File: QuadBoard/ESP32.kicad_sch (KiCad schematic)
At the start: 2 parts, among them J1 Conn_01x06_Pin, U1 ESP32-S3-DevKitC

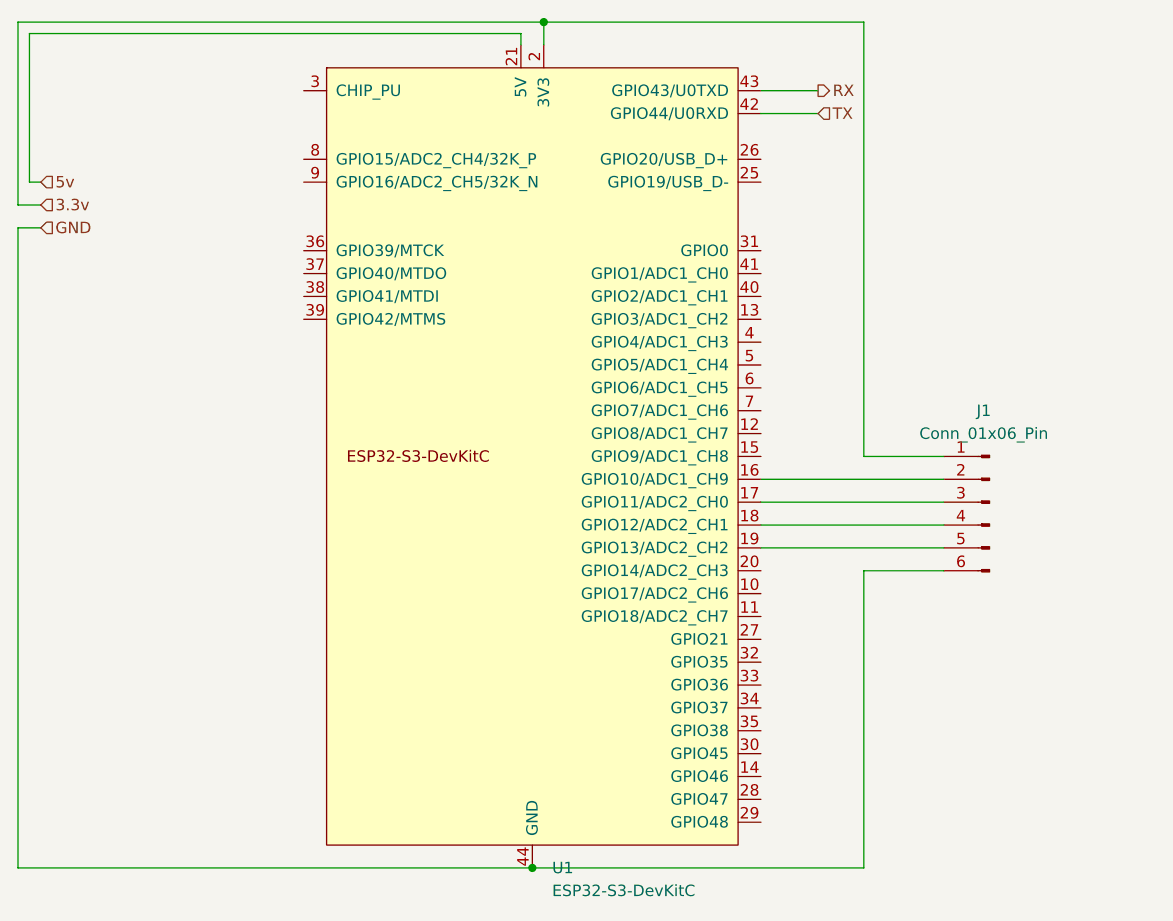
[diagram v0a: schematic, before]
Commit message: Update SD footprint
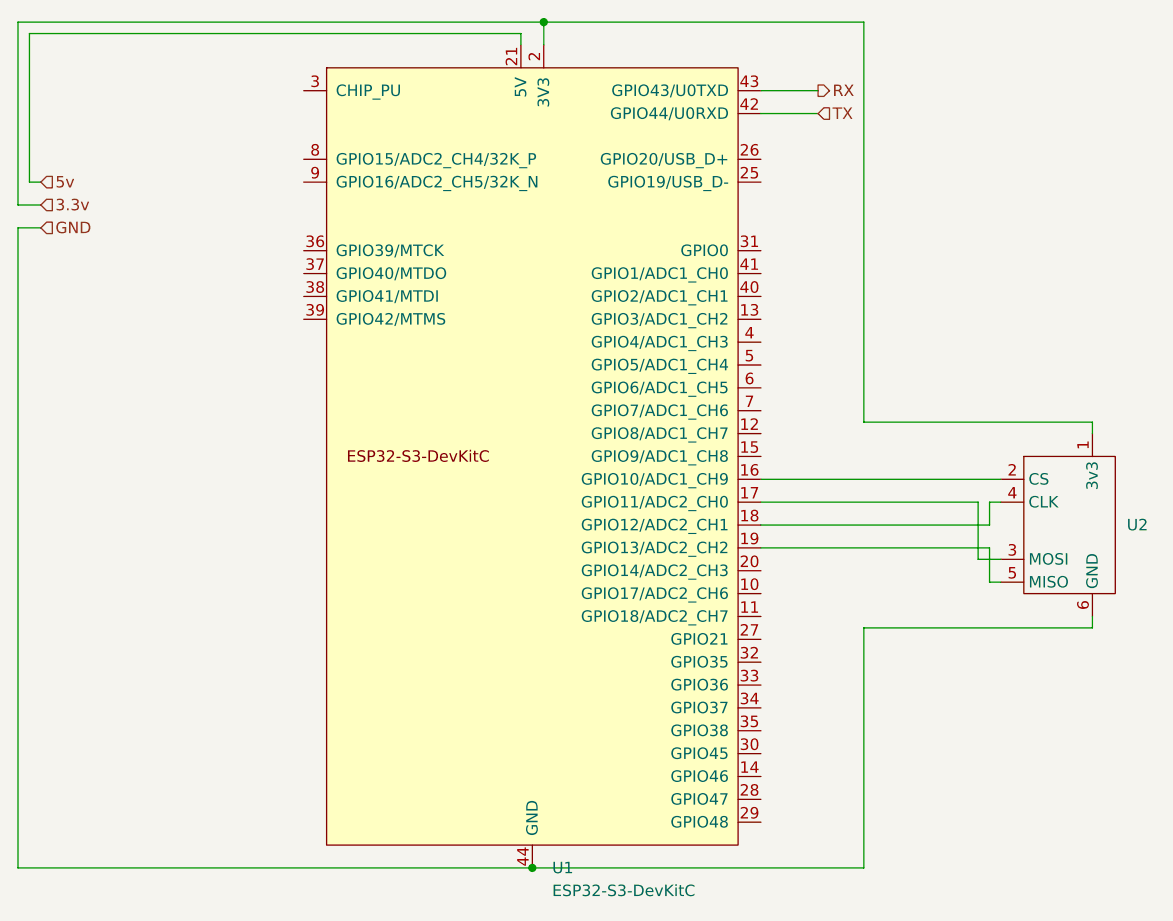
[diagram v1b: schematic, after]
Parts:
- removed J1: Conn_01x06_Pin, Connector_PinHeader_2.54mm:PinHeader_1x06_P2.54mm_Vertical, symbol Connector:Conn_01x06_Pin
- added U2: ~, FlipperLibrary:SD, symbol FlipperLibrary:SD
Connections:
- net 3.3v: now also U2.1 (3v3)
- net GND: now also U2.6 (GND)
- net at U1.16 (GPIO10/ADC1_CH9): now also U2.2 (CS)
- net at U1.17 (GPIO11/ADC2_CH0): now also U2.3 (MOSI)
- net at U1.18 (GPIO12/ADC2_CH1): now also U2.4 (CLK)
- net at U1.19 (GPIO13/ADC2_CH2): now also U2.5 (MISO)
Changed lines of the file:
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@@
   (junction (at 189.23 45.72) (diameter 0) (color 0 0 0 0)
   )
+  (wire (pts (xy 224.79 90.17) (xy 250.19 90.17))
+    (stroke (width 0) (type default))
+  )
   (wire (pts (xy 130.81 45.72) (xy 189.23 45.72))
     (stroke (width 0) (type default))
   )
-  (wire (pts (xy 224.79 93.98) (xy 224.79 45.72))
-    (stroke (width 0) (type default))
-  )
-  (wire (pts (xy 233.68 93.98) (xy 224.79 93.98))
+  (wire (pts (xy 224.79 90.17) (xy 224.79 45.72))
     (stroke (width 0) (type default))
   )
@@
     (stroke (width 0) (type default))
   )
-  (wire (pts (xy 213.36 104.14) (xy 233.68 104.14))
+  (wire (pts (xy 213.36 104.14) (xy 238.76 104.14))
     (stroke (width 0) (type default))
   )
@@
     (stroke (width 0) (type default))
   )
-  (wire (pts (xy 224.79 106.68) (xy 224.79 139.7))
+  (wire (pts (xy 224.79 113.03) (xy 224.79 139.7))
     (stroke (width 0) (type default))
   )
@@
     (stroke (width 0) (type default))
   )
-  (wire (pts (xy 213.36 101.6) (xy 233.68 101.6))
+  (wire (pts (xy 213.36 101.6) (xy 238.76 101.6))
+    (stroke (width 0) (type default))
+  )
+  (wire (pts (xy 238.76 99.06) (xy 240.03 99.06))
     (stroke (width 0) (type default))
   )
@@
     (stroke (width 0) (type default))
   )
-  (wire (pts (xy 233.68 106.68) (xy 224.79 106.68))
-    (stroke (width 0) (type default))
-  )
-  (wire (pts (xy 213.36 99.06) (xy 233.68 99.06))
-    (stroke (width 0) (type default))
-  )
-  (wire (pts (xy 213.36 96.52) (xy 233.68 96.52))
+  (wire (pts (xy 224.79 113.03) (xy 250.19 113.03))
+    (stroke (width 0) (type default))
+  )
+  (wire (pts (xy 238.76 104.14) (xy 238.76 107.95))
+    (stroke (width 0) (type default))
+  )
+  (wire (pts (xy 237.49 105.41) (xy 240.03 105.41))
+    (stroke (width 0) (type default))
+  )
+  (wire (pts (xy 213.36 99.06) (xy 237.49 99.06))
+    (stroke (width 0) (type default))
+  )
+  (wire (pts (xy 250.19 113.03) (xy 250.19 111.76))
+    (stroke (width 0) (type default))
+  )
+  (wire (pts (xy 213.36 96.52) (xy 240.03 96.52))
     (stroke (width 0) (type default))
   )
@@
     (stroke (width 0) (type default))
   )
+  (wire (pts (xy 250.19 90.17) (xy 250.19 91.44))
+    (stroke (width 0) (type default))
+  )
   (wire (pts (xy 130.81 66.04) (xy 130.81 45.72))
     (stroke (width 0) (type default))
   )
+  (wire (pts (xy 237.49 99.06) (xy 237.49 105.41))
+    (stroke (width 0) (type default))
+  )
   (wire (pts (xy 224.79 139.7) (xy 187.96 139.7))
     (stroke (width 0) (type default))
@@
     (stroke (width 0) (type default))
   )
+  (wire (pts (xy 238.76 101.6) (xy 238.76 99.06))
+    (stroke (width 0) (type default))
+  )
+  (wire (pts (xy 238.76 107.95) (xy 240.03 107.95))
+    (stroke (width 0) (type default))
+  )
   (wire (pts (xy 132.08 63.5) (xy 132.08 46.99))
     (stroke (width 0) (type default))
@@
   (hierarchical_label "5v" (shape input) (at 133.35 63.5 0) (fields_autoplaced)
     (effects (font (size 1.27 1.27)) (justify left))
+  )
+  (symbol (lib_id "FlipperLibrary:SD") (at 226.06 93.98 0) (unit 1)
+    (in_bom yes) (on_board yes) (dnp no) (fields_autoplaced)
+    (property "Reference" "U2" (at 254 101.6 0)
+      (effects (font (size 1.27 1.27)) (justify left))
+    )
+    (property "Value" "~" (at 226.06 93.98 0)
+      (effects (font (size 1.27 1.27)))
+    )
+    (property "Footprint" "FlipperLibrary:SD" (at 226.06 93.98 0)
+      (effects (font (size 1.27 1.27)) hide)
+    )
+    (property "Datasheet" "" (at 226.06 93.98 0)
+      (effects (font (size 1.27 1.27)) hide)
+    )
+    (pin "1")
+    (pin "2")
+    (pin "3")
+    (pin "4")
+    (pin "5")
+    (pin "6")
+    (instances
+      (project "QuadBoard"
+        (path "/f483bd80-f513-42f8-b0e7-8ed9a36559bc/ef0ca327-4192-4189-9a0d-e3ab59ce9940"
+          (reference "U2") (unit 1)
+        )
+      )
+    )
   )
   (symbol (lib_id "PCM_Espressif:ESP32-S3-DevKitC") (at 187.96 93.98 0) (unit 1)
@@
     (pin "9")
     (instances
-      (project "FlipperBoard"
+      (project "QuadBoard"
         (path "/f483bd80-f513-42f8-b0e7-8ed9a36559bc/ef0ca327-4192-4189-9a0d-e3ab59ce9940"
           (reference "U1") (unit 1)
         )
       )
-    )
-  )
-  (symbol (lib_id "Connector:Conn_01x06_Pin") (at 238.76 99.06 0) (mirror y) (unit 1)
-    (in_bom yes) (on_board yes) (dnp no)
-    (property "Reference" "J1" (at 238.125 88.9 0)
-      (effects (font (size 1.27 1.27)))
-    )
-    (property "Value" "Conn_01x06_Pin" (at 238.125 91.44 0)
-      (effects (font (size 1.27 1.27)))
-    )
-    (property "Footprint" "Connector_PinHeader_2.54mm:PinHeader_1x06_P2.54mm_Vertical" (at 238.76 99.06 0)
-      (effects (font (size 1.27 1.27)) hide)
-    )
-    (property "Datasheet" "~" (at 238.76 99.06 0)
-      (effects (font (size 1.27 1.27)) hide)
-    )
-    (pin "1")
-    (pin "2")
-    (pin "3")
-    (pin "4")
-    (pin "5")
-    (pin "6")
-    (instances
-      (project "FlipperBoard"
-        (path "/f483bd80-f513-42f8-b0e7-8ed9a36559bc/ef0ca327-4192-4189-9a0d-e3ab59ce9940"
-          (reference "J1") (unit 1)
-        )
-      )
